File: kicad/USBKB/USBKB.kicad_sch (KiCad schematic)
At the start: 70 parts, among them U1 USB4105-GF-A, U2 ICSP, U3 ATMEGA32U4-MU, Y1 Crystal_GND23

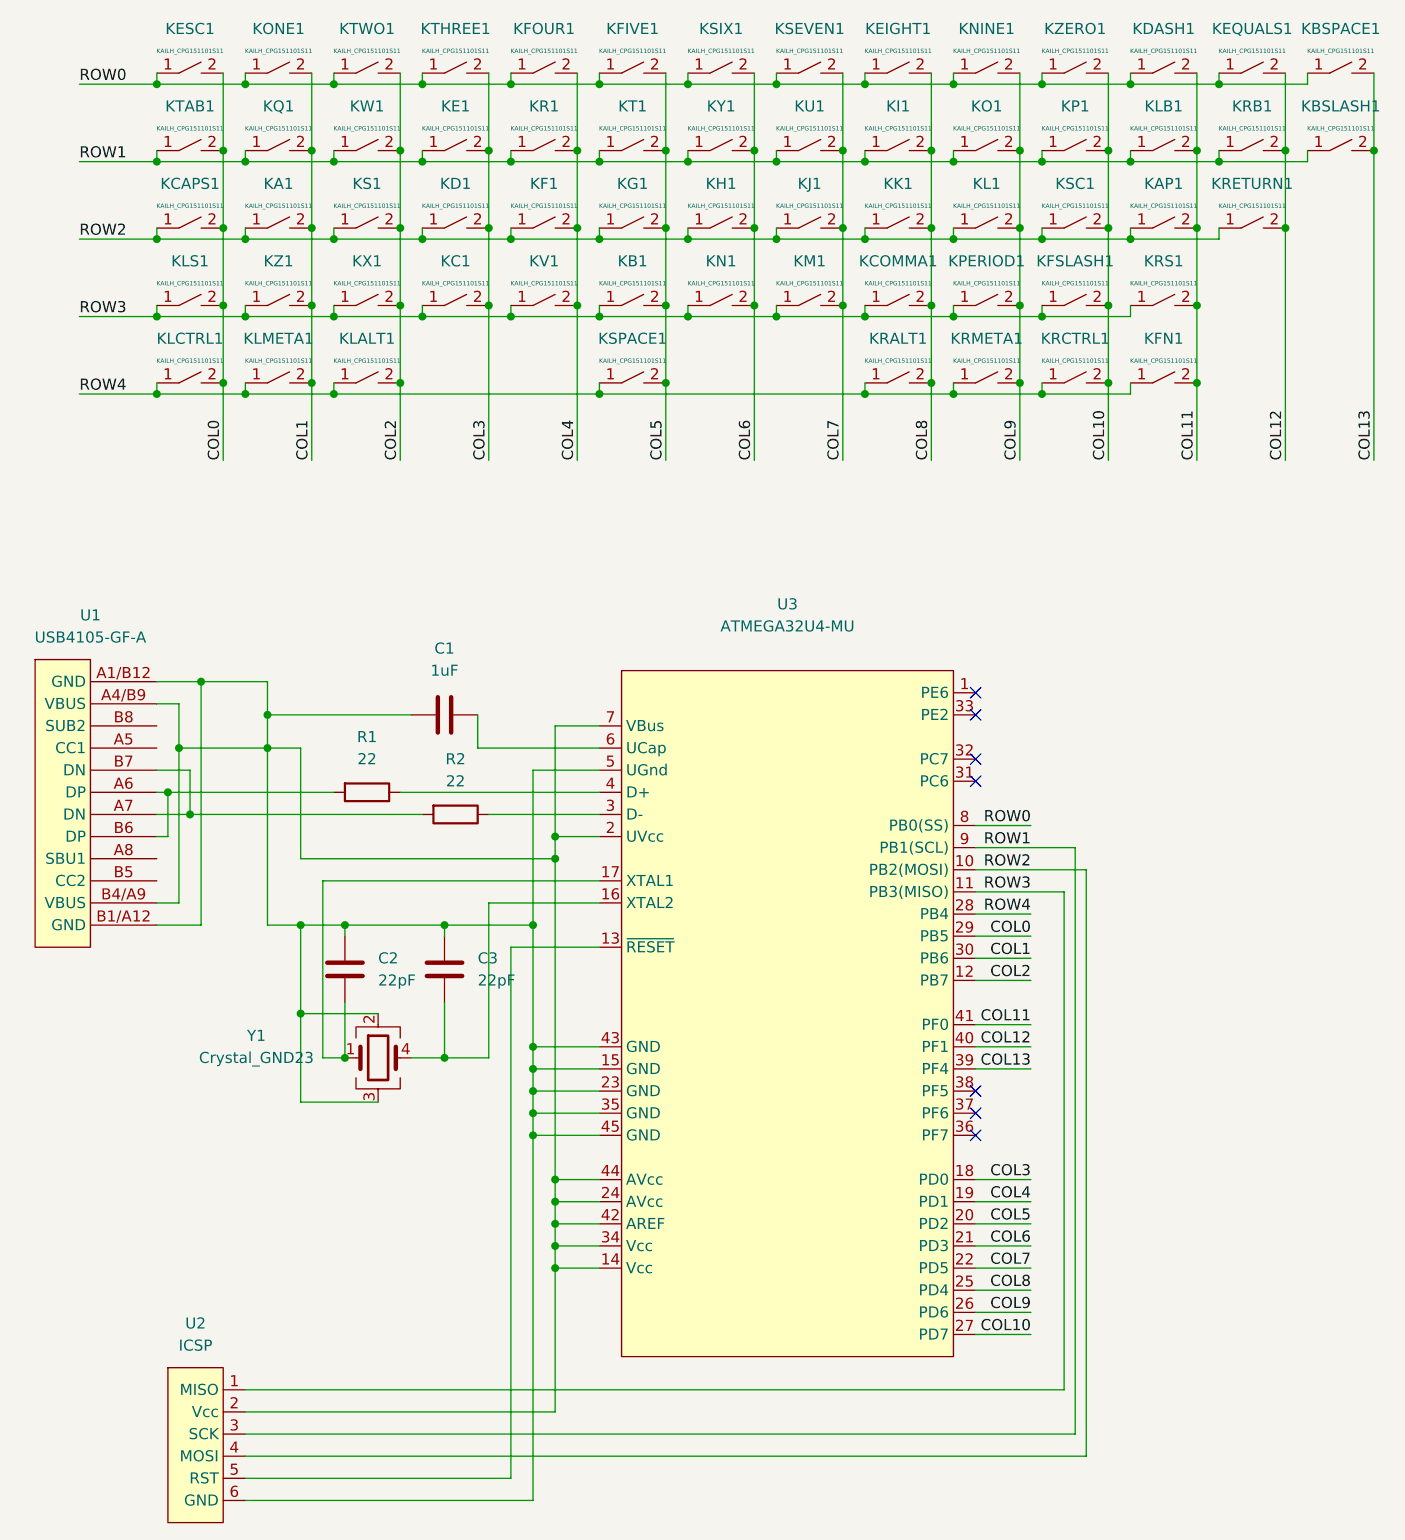
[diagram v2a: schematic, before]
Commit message: Plate and PCB completed, pricing list updated with shipping fees
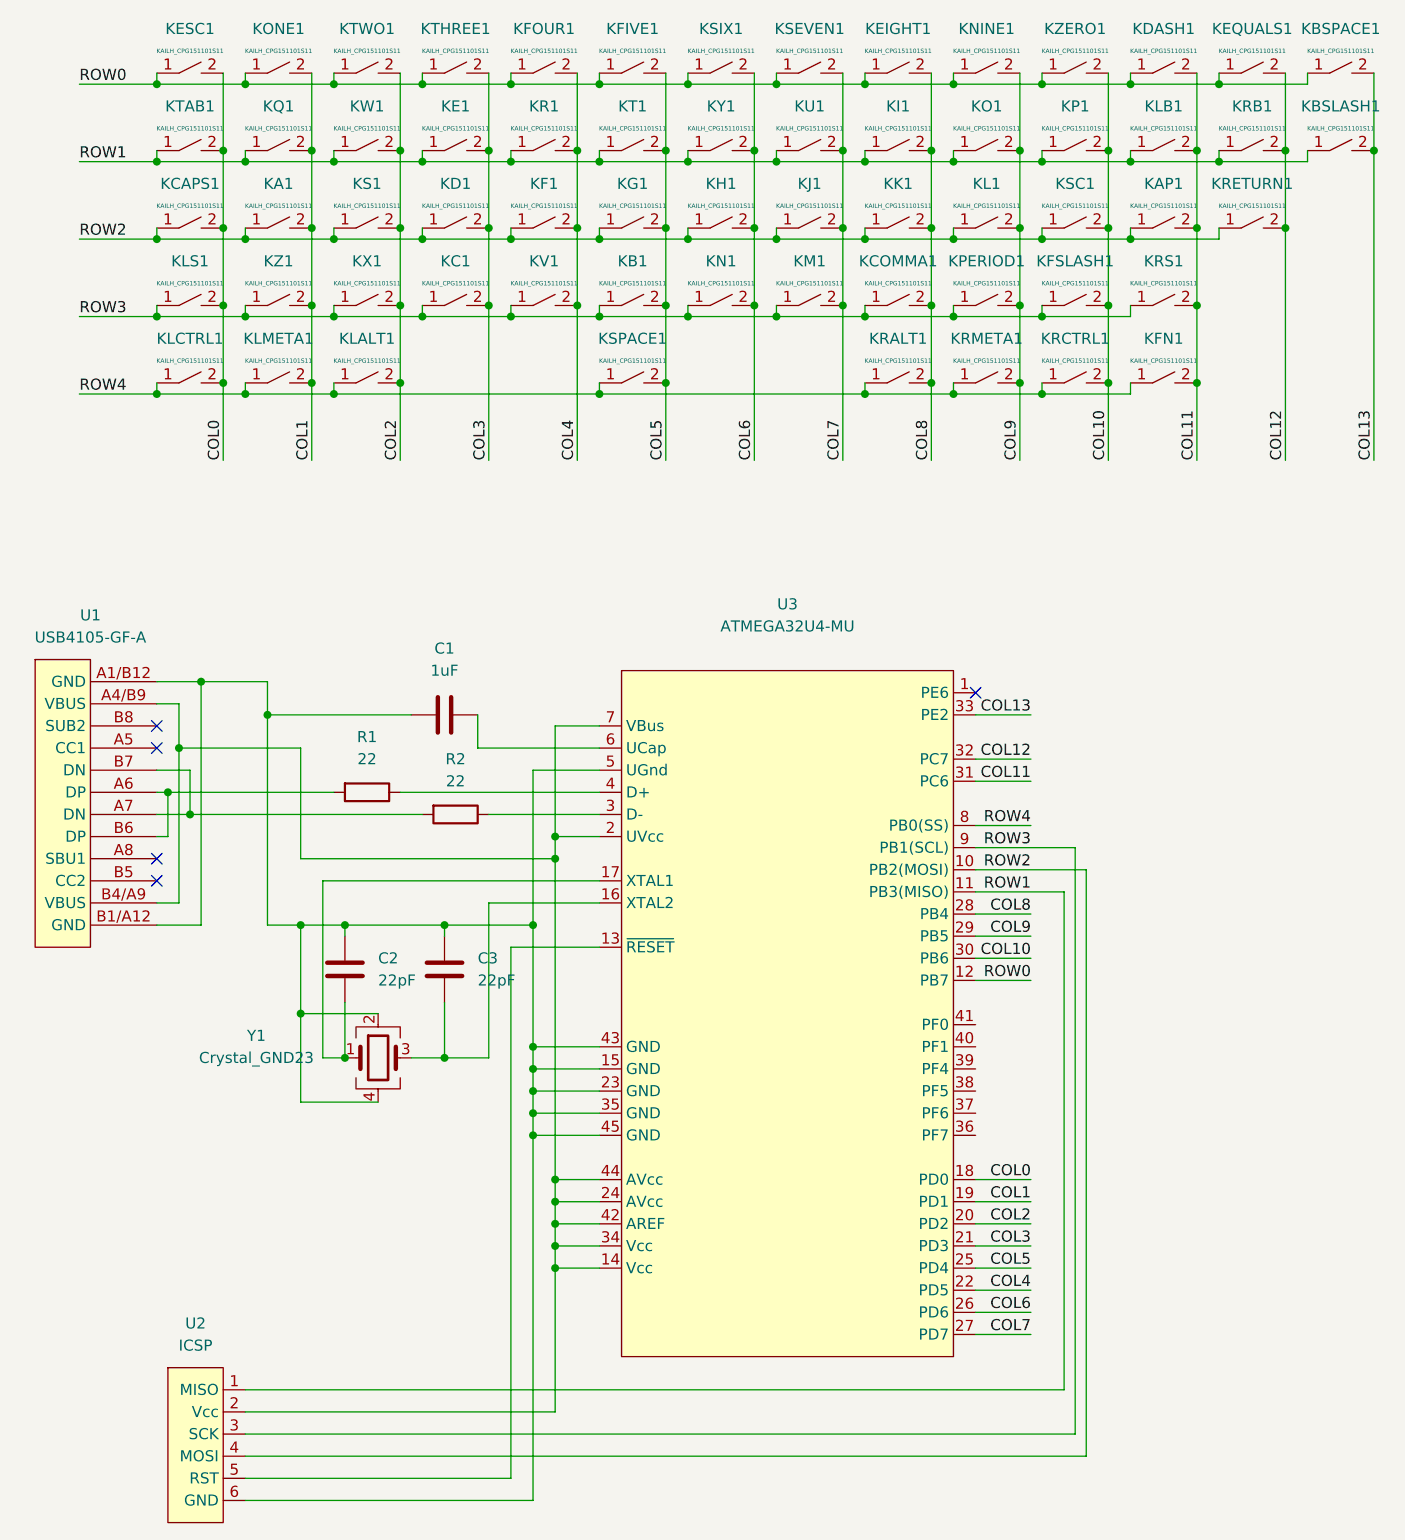
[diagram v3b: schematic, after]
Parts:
- Y1: symbol Device:Crystal_GND23 -> Device:Crystal_GND24
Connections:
- net COL0: now also U3.18 (PD0); no longer U3.29 (PB5)
- net COL1: now also U3.19 (PD1); no longer U3.30 (PB6)
- net COL10: now also U3.30 (PB6); no longer U3.27 (PD7)
- net COL11: now also U3.31 (PC6); no longer U3.41 (PF0)
- net COL12: now also U3.32 (PC7); no longer U3.40 (PF1)
- net COL13: now also U3.33 (PE2); no longer U3.39 (PF4)
- net COL2: now also U3.20 (PD2); no longer U3.12 (PB7)
- net COL3: now also U3.21 (PD3); no longer U3.18 (PD0)
- net COL4: now also U3.22 (PD5); no longer U3.19 (PD1)
- net COL5: now also U3.25 (PD4); no longer U3.20 (PD2)
- net COL6: now also U3.26 (PD6); no longer U3.21 (PD3)
- net COL7: now also U3.27 (PD7); no longer U3.22 (PD5)
- net COL8: now also U3.28 (PB4); no longer U3.25 (PD4)
- net COL9: now also U3.29 (PB5); no longer U3.26 (PD6)
- net ROW0: now also U3.12 (PB7); no longer U3.8 (PB0(SS))
- net ROW1: now also U2.1 (MISO), U3.11 (PB3(MISO)); no longer U2.3 (SCK), U3.9 (PB1(SCL))
- net ROW3: now also U2.3 (SCK), U3.9 (PB1(SCL)); no longer U2.1 (MISO), U3.11 (PB3(MISO))
- net ROW4: now also U3.8 (PB0(SS)); no longer U3.28 (PB4)
- net at C1.1, C2.1, C3.1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: now also Y1.4; no longer U1.A4/B9 (VBUS), U1.B4/A9 (VBUS), U2.2 (Vcc), U3.14 (Vcc), U3.2 (UVcc), U3.24 (AVcc), U3.34 (Vcc), U3.42 (AREF), U3.44 (AVcc), U3.7 (VBus), Y1.3
- net at C3.2, U3.16 (XTAL2): now also Y1.3; no longer Y1.4
- new net: U1.A4/B9 (VBUS), U1.B4/A9 (VBUS), U2.2 (Vcc), U3.14 (Vcc), U3.2 (UVcc), U3.24 (AVcc), U3.34 (Vcc), U3.42 (AREF), U3.44 (AVcc), U3.7 (VBus)
- no-connect marks 7 -> 5
